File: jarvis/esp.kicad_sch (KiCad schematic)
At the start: 32 parts, among them IC1 ESP32-S3R16V, Y1 Crystal 32.768khz, Y2 Crystal 40mhz

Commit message: crystals done
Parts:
- removed Y1: Crystal 32.768khz, jarvis:XTAL_CM8V-T1A-32.768KHZ-7PF-20PPM-TA-QC, symbol jarvis:CM8V-T1A-32.768KHZ-7PF-20PPM-TA-QC
- removed Y2: Crystal 40mhz, jarvis:XTAL_CM8V-T1A-32.768KHZ-7PF-20PPM-TA-QC, symbol jarvis:CM8V-T1A-32.768KHZ-7PF-20PPM-TA-QC
- added Y2: ABM10W-40.0000MHZ-8-N1G-T3, jarvis:XTAL_ABM10W-40.0000MHZ-8-N1G-T3, symbol jarvis:ABM10W-40.0000MHZ-8-N1G-T3
- added Y3: ECS-.327-12.5-1210B-N-TR, jarvis:XTAL_ECS-.327-12.5-1210B-N-TR, symbol jarvis:ECS-.327-12.5-1210B-N-TR
- C10, C9: value 12pf -> 12.5pf
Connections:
- net GND: now also Y2.2 (GND), Y2.4 (GND__1), Y3.2
- net at C16.1, IC1.53 (XTAL_N): now also Y2.3
- net at C9.1, IC1.21 (XTAL_32K_P), R7.1: now also Y3.1
- net at C10.1, IC1.22 (XTAL_32K_N), R7.2: now also Y3.3
- net at C14.2, L1.2: now also Y2.1
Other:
- moved on the sheet: C10, C14, C16

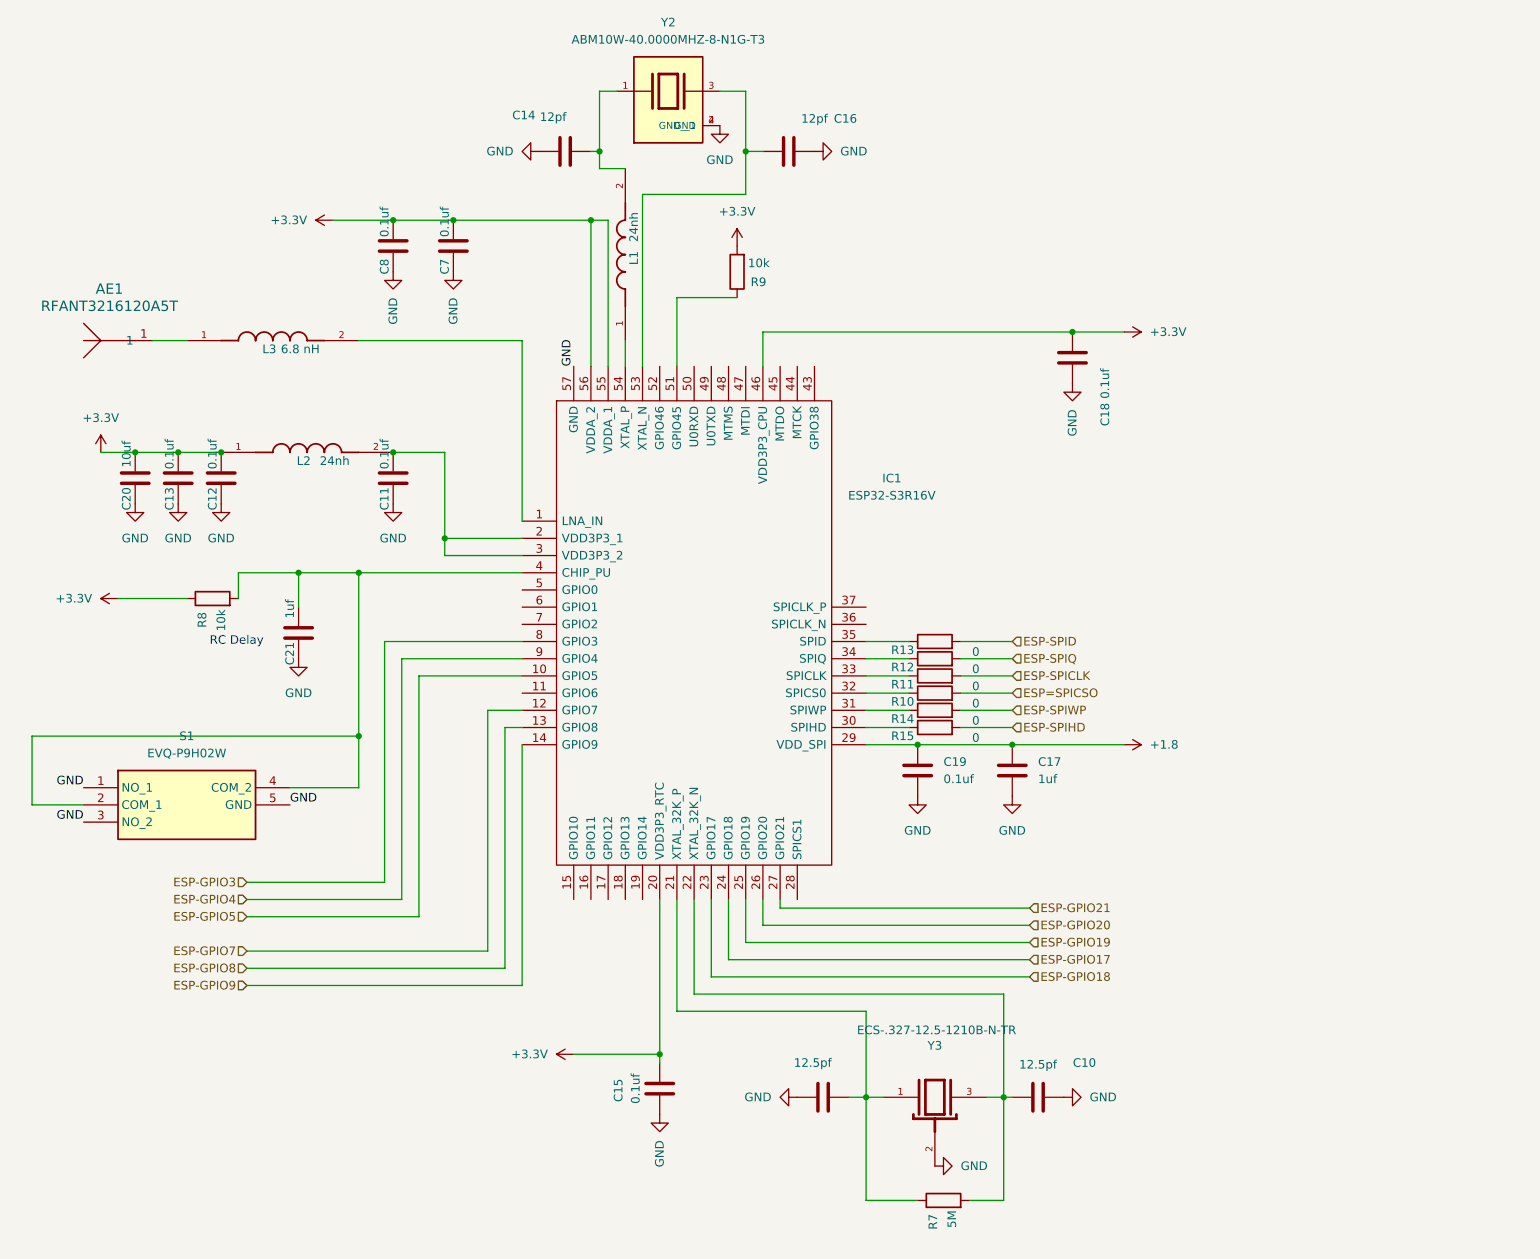
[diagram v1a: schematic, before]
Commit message: with leds and boot button
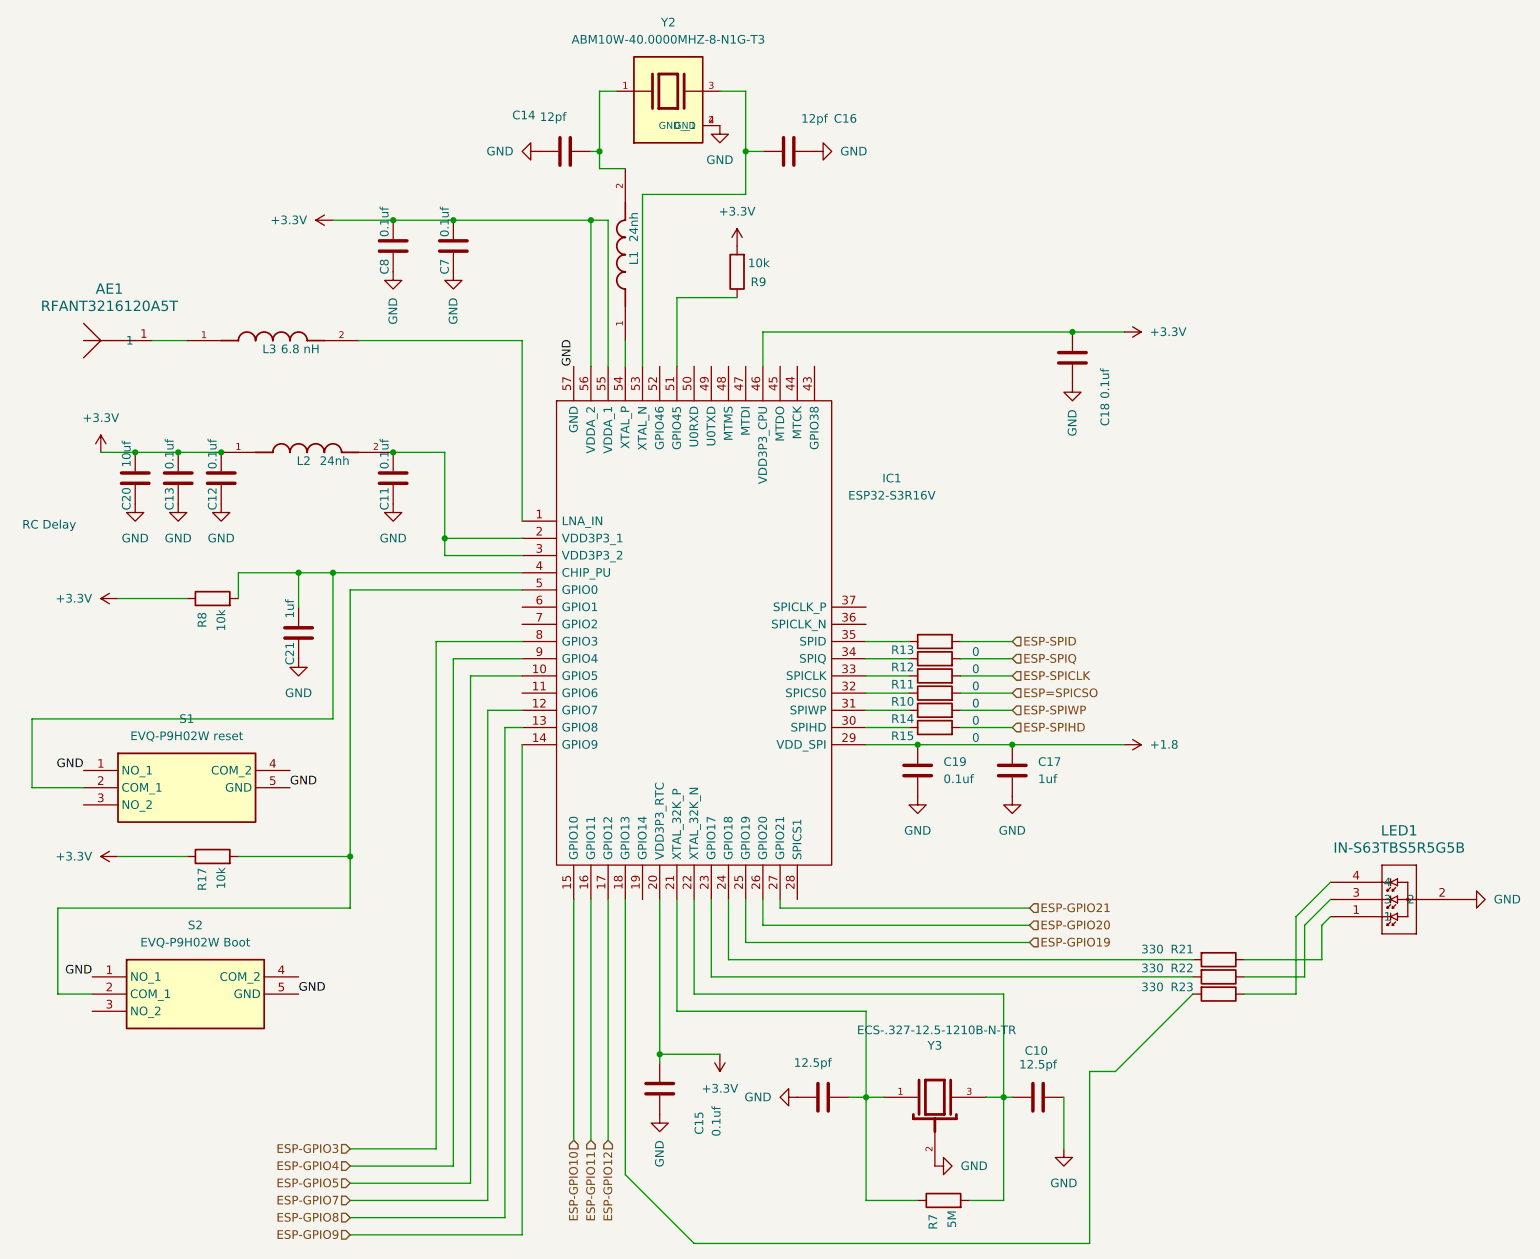
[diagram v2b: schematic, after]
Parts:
- added LED1: IN-S63TBS5R5G5B, jarvis:IN-S63TBS5R5G5B_INO, symbol jarvis:IN-S63TBS5R5G5B
- added R17: 10k, Resistor_SMD:R_0603_1608Metric, symbol Device:R
- added R21, R22, R23: 330, Resistor_SMD:R_0603_1608Metric, symbol Device:R
- added S2: EVQ-P9H02W Boot, jarvis:EVQP9H02W, symbol jarvis:EVQ-P9H02W
- L3: footprint Inductor_SMD:L_01005_0402Metric -> jarvis:MLG1005SR24JT000
- S1: value EVQ-P9H02W -> EVQ-P9H02W reset
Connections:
- net +3.3V: now also R17.1
- net GND: now also LED1.2, S2.1 (NO_1), S2.5 (GND); no longer S1.3 (NO_2)
- net at C21.1, IC1.4 (CHIP_PU), R8.2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: no longer S1.4 (COM_2)
- net ESP-GPIO10: now reaches IC1.15 (GPIO10)
- net ESP-GPIO11: now reaches IC1.16 (GPIO11)
- net ESP-GPIO12: now reaches IC1.17 (GPIO12)
- net at IC1.18 (GPIO13): now also R23.2
- net at IC1.5 (GPIO0): now also R17.2, S2.2 (COM_1)
- net ESP-GPIO17: no longer names the net of IC1.24 (GPIO18)
- net ESP-GPIO17: now also R21.2
- net ESP-GPIO18: no longer names the net of IC1.23 (GPIO17)
- net ESP-GPIO18: now also R22.2
- new net: LED1.1, R21.1
- new net: LED1.3, R22.1
- new net: LED1.4, R23.1
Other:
- moved on the sheet: S1

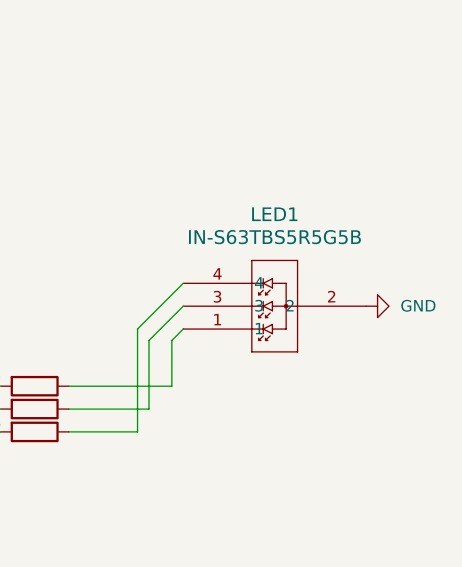
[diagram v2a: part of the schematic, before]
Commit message: small fixes from testing new pcb swap d lines connected pins on power ic that needed to be changed rbg led to be common anode
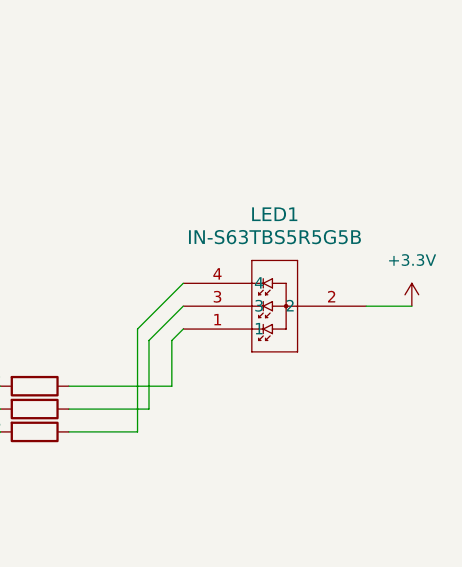
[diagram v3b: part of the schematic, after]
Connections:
- net +3.3V: now also LED1.2
- net GND: no longer LED1.2
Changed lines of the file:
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@@
 	(wire
 		(pts
+			(xy 229.87 142.24) (xy 234.95 142.24)
+		)
+		(stroke
+			(width 0)
+			(type default)
+		)
+	)
+	(wire
+		(pts
 			(xy 100.33 41.91) (xy 80.01 41.91)
 		)
@@
 	)
 	(symbol
-		(lib_id "power:GND")
-		(at 229.87 142.24 90)
-		(unit 1)
-		(exclude_from_sim no)
-		(in_bom yes)
-		(on_board yes)
-		(dnp no)
-		(fields_autoplaced yes)
-		(property "Reference" "#PWR050"
-			(at 236.22 142.24 0)
-			(effects
-				(font
-					(size 1.27 1.27)
-				)
-				(hide yes)
-			)
-		)
-		(property "Value" "GND"
-			(at 233.68 142.2399 90)
-			(effects
-				(font
-					(size 1.27 1.27)
-				)
-				(justify right)
-			)
-		)
-		(property "Footprint" ""
-			(at 229.87 142.24 0)
-			(effects
-				(font
-					(size 1.27 1.27)
-				)
-				(hide yes)
-			)
-		)
-		(property "Datasheet" ""
-			(at 229.87 142.24 0)
-			(effects
-				(font
-					(size 1.27 1.27)
-				)
-				(hide yes)
-			)
-		)
-		(property "Description" "Power symbol creates a global label with name \"GND\" , ground"
-			(at 229.87 142.24 0)
-			(effects
-				(font
-					(size 1.27 1.27)
-				)
-				(hide yes)
-			)
-		)
-		(pin "1"
-		)
-		(instances
-			(project "jarvis"
-				(path "/d21d45e5-a4fd-47b9-acaa-6ca2c284b61a/66ec1c32-4132-43c8-99e8-65f1381b5871"
-					(reference "#PWR050")
-					(unit 1)
-				)
-			)
-		)
-	)
-	(symbol
 		(lib_id "Device:C")
 		(at 96.52 31.75 90)
@@
 					(unit 1)
 				)
+			)
+		)
+	)
+	(symbol
+		(lib_id "power:+3.3V")
+		(at 234.95 142.24 0)
+		(unit 1)
+		(exclude_from_sim no)
+		(in_bom yes)
+		(on_board yes)
+		(dnp no)
+		(fields_autoplaced yes)
+		(property "Reference" "#PWR051"
+			(at 234.95 146.05 0)
+			(effects
+				(font
+					(size 1.27 1.27)
+				)
+				(hide yes)
+			)
+		)
+		(property "Value" "+3.3V"
+			(at 234.95 137.16 0)
+			(effects
+				(font
+					(size 1.27 1.27)
+				)
+			)
+		)
+		(property "Footprint" ""
+			(at 234.95 142.24 0)
+			(effects
+				(font
+					(size 1.27 1.27)
+				)
+				(hide yes)
+			)
+		)
+		(property "Datasheet" ""
+			(at 234.95 142.24 0)
+			(effects
+				(font
+					(size 1.27 1.27)
+				)
+				(hide yes)
+			)
+		)
+		(property "Description" "Power symbol creates a global label with name \"+3.3V\""
+			(at 234.95 142.24 0)
+			(effects
+				(font
+					(size 1.27 1.27)
+				)
+				(hide yes)
+			)
+		)
+		(pin "1"
+		)
+		(instances
+			(project ""
+				(path "/d21d45e5-a4fd-47b9-acaa-6ca2c284b61a/66ec1c32-4132-43c8-99e8-65f1381b5871"
+					(reference "#PWR051")
+					(unit 1)
+				)
